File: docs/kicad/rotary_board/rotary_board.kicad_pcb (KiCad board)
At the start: 2 copper layers, 110 x 30 mm, 8 parts, among them J1 Conn_01x05, SW1 ROT1, SW2 ROT2, SW3 ROT3, SW4 ROT4, U1 mcp23017

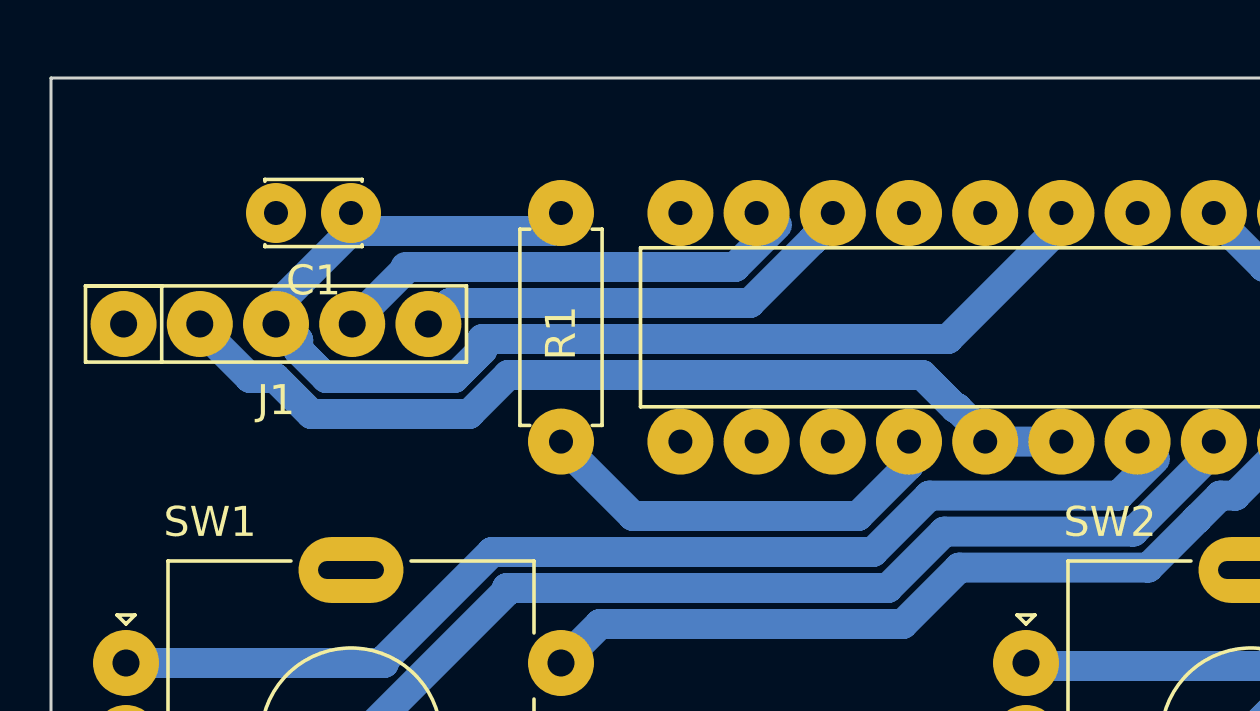
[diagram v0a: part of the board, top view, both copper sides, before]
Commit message: added kicad led_board, updated mother board RCA socket
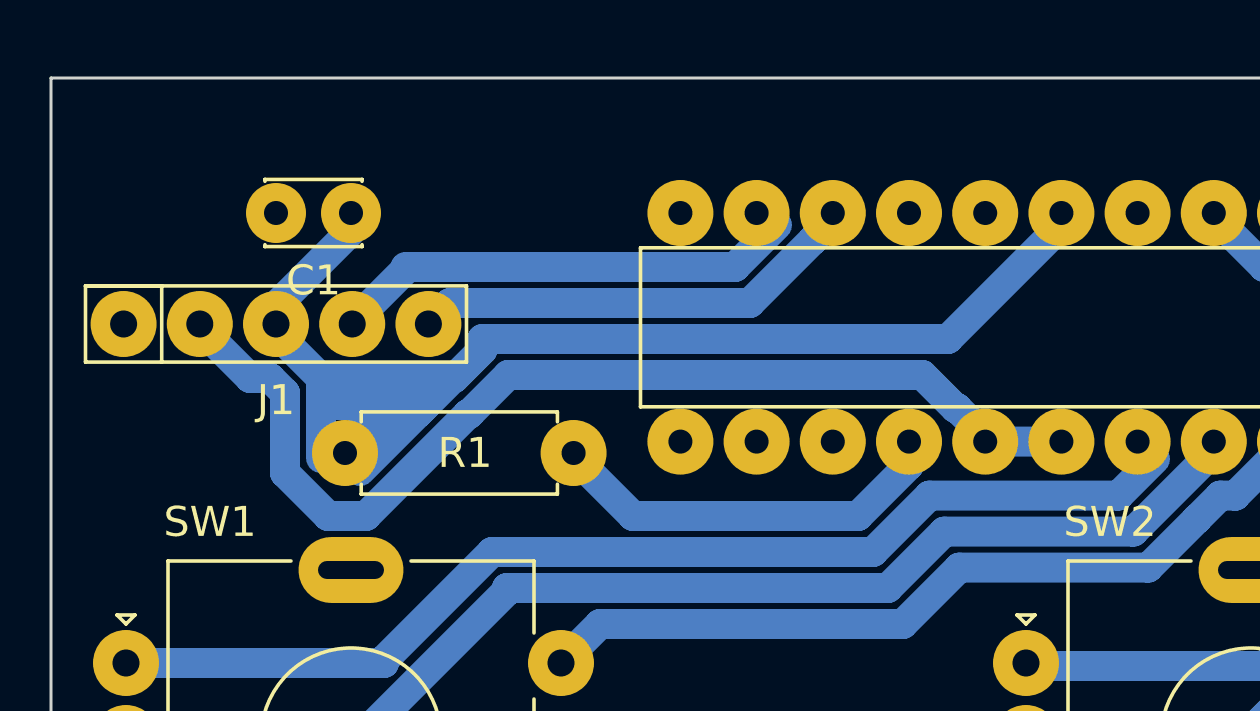
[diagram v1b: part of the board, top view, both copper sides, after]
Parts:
- moved R1 10.8 mm to (59.8, 90.5), turned to 0 degrees
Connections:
- SW1 pad : (no net) -> GND
- SW2 pad : (no net) -> GND
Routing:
- net +3V3: track 40.5 -> 45.6 mm
- net ROT_INT: track 31.3 -> 36.3 mm

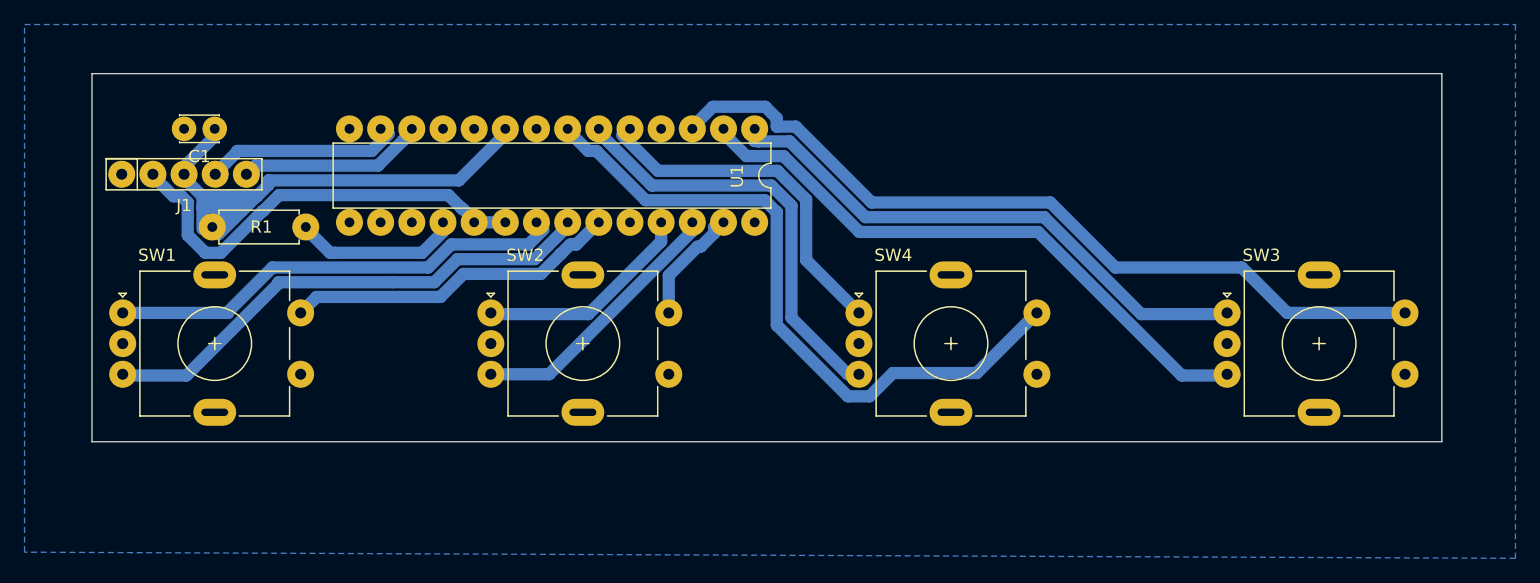
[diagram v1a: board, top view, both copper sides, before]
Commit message: PCB milling marathon - made 5 row_boards, rotary_board, led_board, and reworked detailed design of motherboard - motherboard *should* match old one that was milled and installed in initial TE3 box
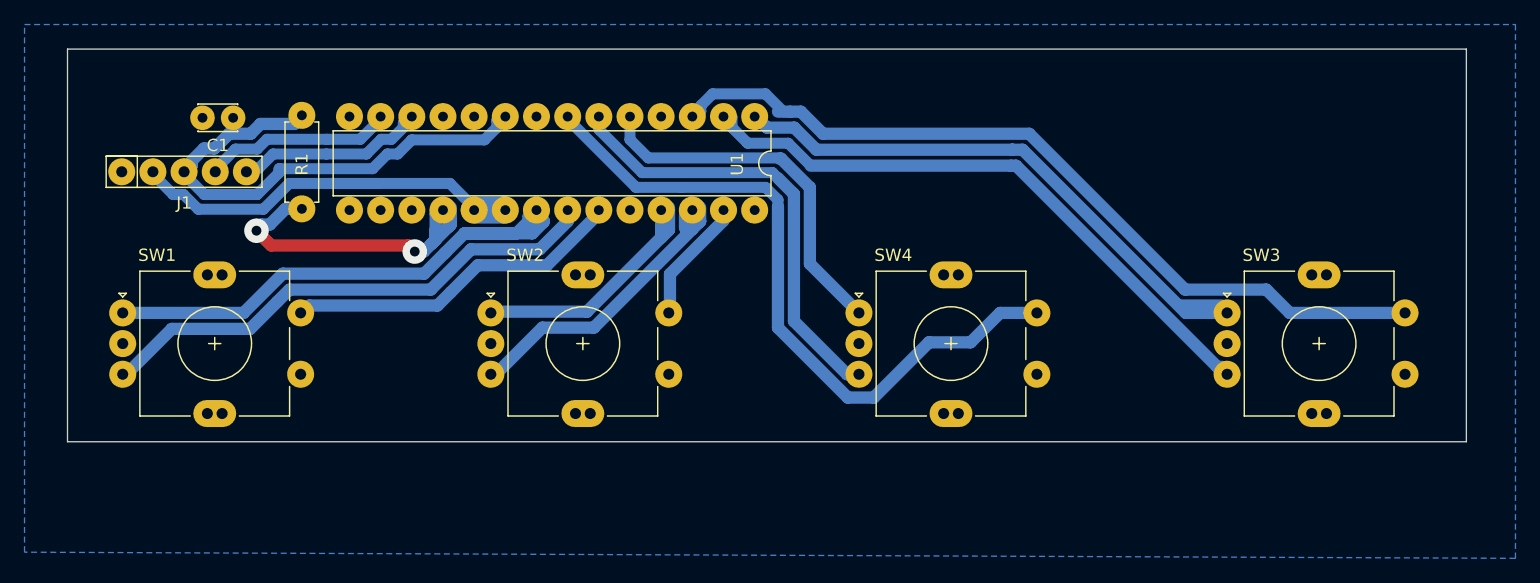
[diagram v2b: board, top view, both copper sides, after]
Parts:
- moved R1 11.7 mm to (67.1, 81.4), turned to 270 degrees
- moved C1 1.75 mm to (61.5, 81.6)
- moved U1 1.00 mm to (104.0, 81.5)
- moved J1 0.20 mm to (57.5, 86.0)
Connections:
- SW1 pad : GND -> (no net)
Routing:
- net Net-(R1-Pad2): track 14.1 -> 29.2 mm, vias 0 -> 2
- net ROT1A: track 37.3 -> 45.7 mm
- net ROT2B: track 22.0 -> 25.9 mm
- net ROT2A: track 17.8 -> 21.7 mm
- net ROT3A: track 45.3 -> 48.4 mm
- net +3V3: track 45.6 -> 43.2 mm
- net ROT4A: track 28.2 -> 30.2 mm
- net ROT3B: track 49.6 -> 51.3 mm
- net ROT4B: track 34.9 -> 36.6 mm
- net SW4: track 55.5 -> 56.8 mm
- net SW3: track 66.3 -> 67.5 mm
- net SW1: track 27.1 -> 27.8 mm
- net SW2: track 9.60 -> 10.3 mm
- net ROT_INT: track 36.3 -> 35.7 mm
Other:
- board size 110 x 30 mm -> 114 x 32 mm
- net class Default: clearance 0.2 -> 0.3
- rule trace_clearance: 0.2 -> 0.3

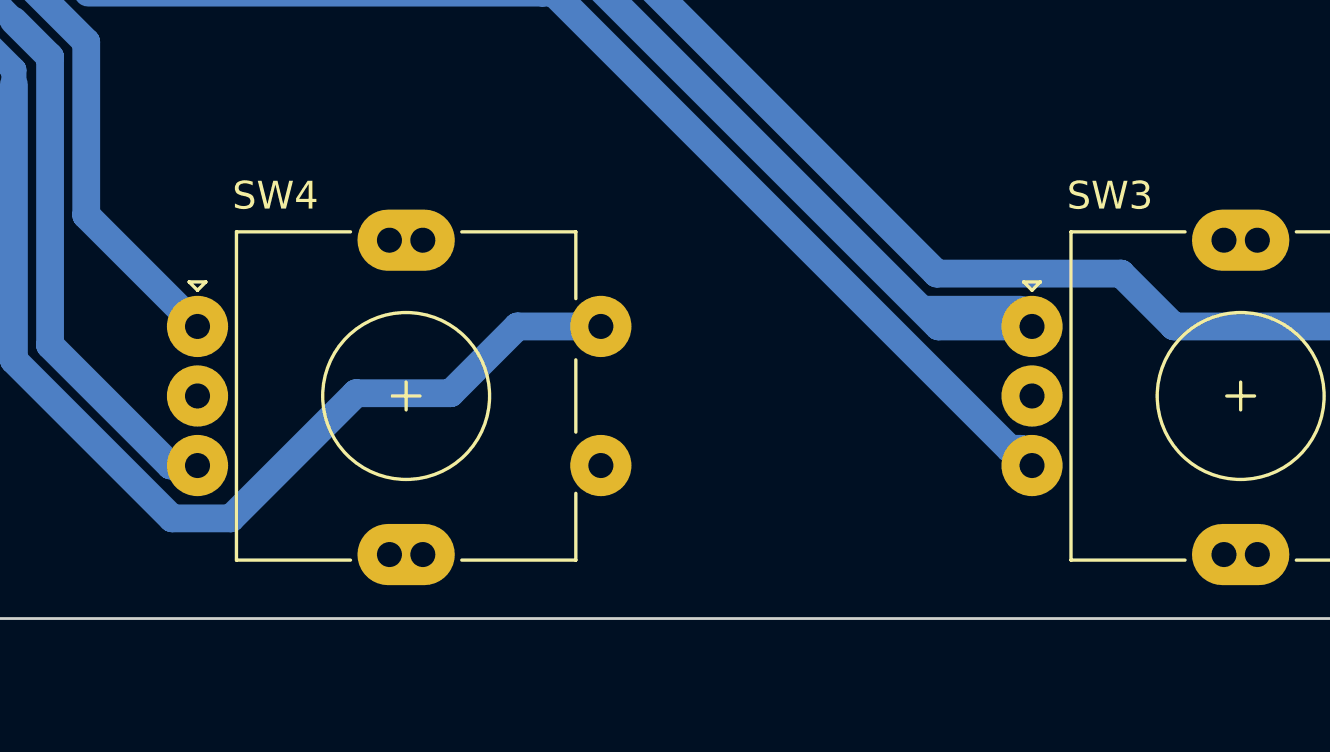
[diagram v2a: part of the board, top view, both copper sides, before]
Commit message: final initial TE3 PCBS - updated LED board green resistor to 1K - changed TE3 display SCLK to pin13 as it is required for hardware SPI0 - changed nomenclature of rotary board to ROT0..ROT4 and corrected order to match named rotary 1..4
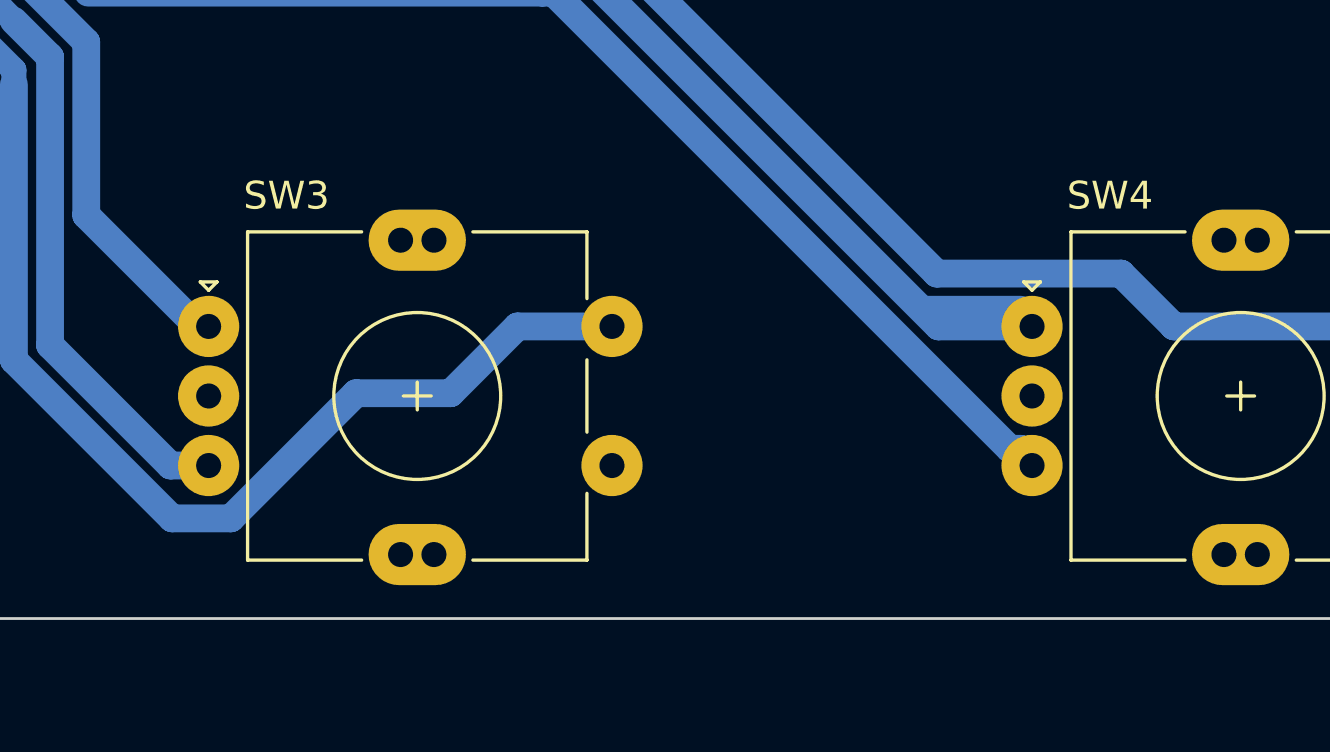
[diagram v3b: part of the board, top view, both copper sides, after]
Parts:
- moved SW4 30.0 mm to (150.0, 100.0)
- moved SW3 29.6 mm to (120.4, 100.0)
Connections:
- SW1 pad A: ROT1A -> ROT0A
- SW1 pad B: ROT1B -> ROT0B
- SW1 pad S1: SW1 -> SW0
- SW2 pad : GND -> (no net)
- SW2 pad A: ROT2A -> ROT1A
- SW2 pad B: ROT2B -> ROT1B
- SW2 pad S1: SW2 -> SW1
- SW3 pad A: ROT3A -> ROT2A
- SW3 pad B: ROT3B -> ROT2B
- SW3 pad S1: SW3 -> SW2
- SW4 pad A: ROT4A -> ROT3A
- SW4 pad B: ROT4B -> ROT3B
- SW4 pad S1: SW4 -> SW3
- U1 pad 21: ROT1A -> ROT0A
- U1 pad 22: ROT1B -> ROT0B
- U1 pad 23: SW1 -> SW0
- U1 pad 25: ROT2A -> ROT1A
- U1 pad 26: ROT2B -> ROT1B
- U1 pad 27: SW2 -> SW1
- U1 pad 5: ROT4A -> ROT2A
- U1 pad 6: ROT4B -> ROT2B
- U1 pad 7: SW4 -> SW2
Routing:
- net SW4: track 56.8 -> 0.00 mm
- net SW2: track 10.3 -> 56.8 mm
- net ROT0A: track 0.00 -> 45.7 mm
- net ROT0B: track 0.00 -> 42.3 mm
- net ROT4B: track 36.6 -> 0.00 mm
- net ROT4A: track 30.2 -> 0.00 mm
- net SW0: track 0.00 -> 27.8 mm
- net ROT1A: track 45.7 -> 21.7 mm
- net SW1: track 27.8 -> 10.3 mm
- net ROT1B: track 42.3 -> 25.9 mm
- net ROT2B: track 25.9 -> 36.6 mm
- net ROT2A: track 21.7 -> 30.2 mm
